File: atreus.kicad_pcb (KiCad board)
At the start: 2 copper layers, 232 x 90 mm, 85 parts

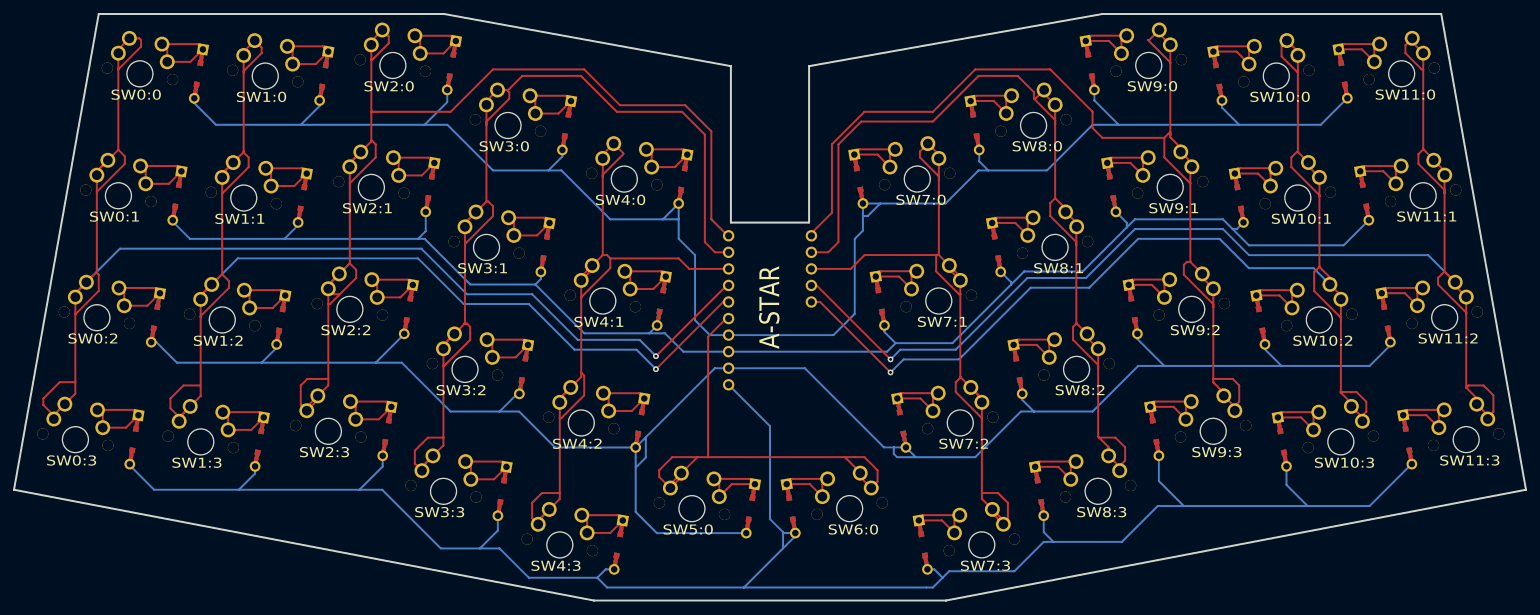
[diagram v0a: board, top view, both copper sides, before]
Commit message: Some Changes:
- Replaced Pololu A-Star with ProMicro.
- Replaced switch footprint with Keebio's switch footprint.
  - Now supports MX, Alps, and Choc.
- Replaced diode footprint with Keebio's switch footprint.
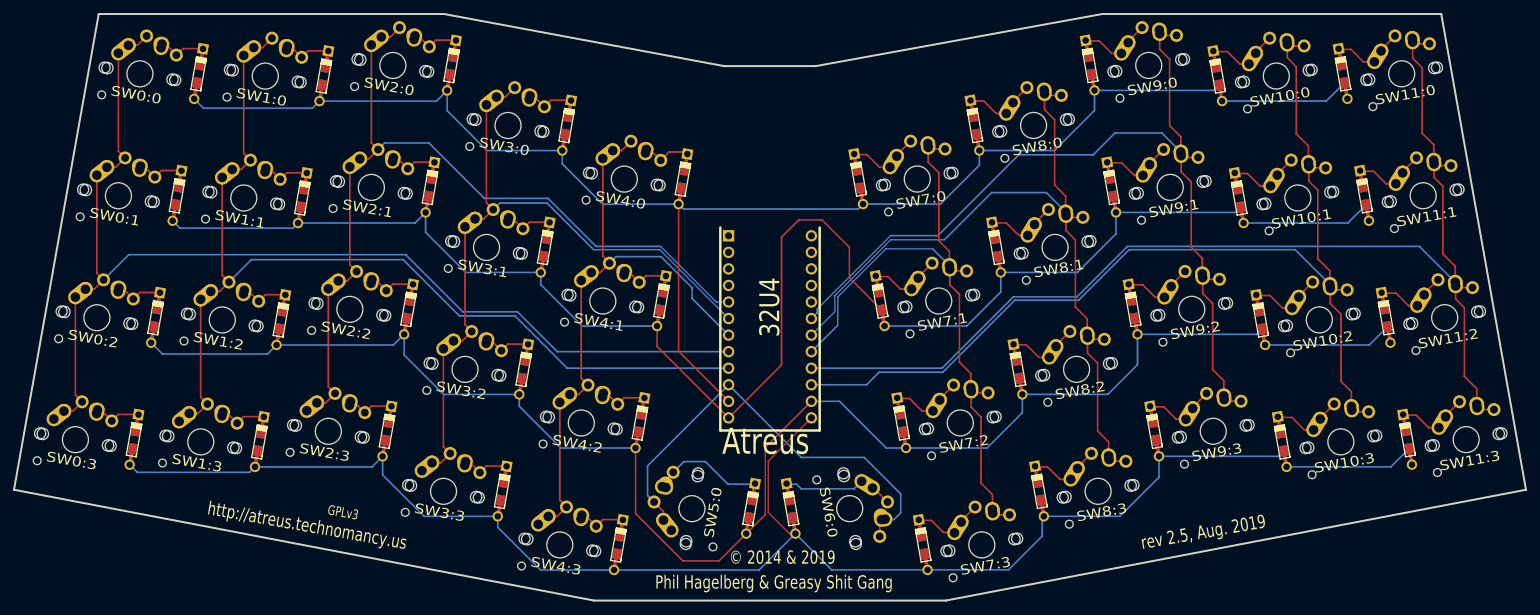
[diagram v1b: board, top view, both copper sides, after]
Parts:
- ?: value A-STAR -> 32U4; footprint A_STAR -> PROMICRO
- SW0:0, SW0:1, SW0:2, SW0:3, SW10:0, SW10:1, SW10:2, SW10:3, SW11:0, SW11:1, SW11:2, SW11:3, SW1:0, SW1:1, SW1:2, SW1:3, SW2:0, SW2:1, SW2:2, SW2:3, SW3:0, SW3:1, SW3:2, SW3:3, SW4:0, SW4:1, SW4:2, SW4:3, SW5:0, SW6:0, SW7:0, SW7:1, SW7:2, SW7:3, SW8:0, SW8:1, SW8:2, SW8:3, SW9:0, SW9:1, SW9:2, SW9:3: footprint MX_FLIP -> Keebio-Parts:MX-Alps-Choc-1U-NoLED
- turned SW5:0 to 80 degrees
- turned SW6:0 to 280 degrees
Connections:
- ? pad B4: N-col-3 -> N-row-0
- ? pad B5: N-col-2 -> N-row-1
- ? pad B6: N-col-6 -> N-row-3
- ? pad C6: N-col-1 -> N-col-0
- ? pad D0: N-row-0 -> N-col-3
- ? pad D1: N-row-1 -> N-col-2
- ? pad D4: N-col-5 -> N-col-4
- ? pad D7: N-col-0 -> N-col-1
- ? pad E6: N-col-4 -> N-col-5
- ? pad F7: N-col-8 -> N-col-6
- D2:2 pad 1: N-row-0 -> N-diode-0
- D2:2 pad 2: N-diode-0 -> N-row-0
- D2:2 pad 1: N-row-1 -> N-diode-9
- D2:2 pad 2: N-diode-9 -> N-row-1
- D2:2 pad 1: N-row-2 -> N-diode-10
- D2:2 pad 2: N-diode-10 -> N-row-2
- D2:2 pad 1: N-row-3 -> N-diode-11
- D2:2 pad 2: N-diode-11 -> N-row-3
- D2:2 pad 1: N-row-0 -> N-diode-12
- D2:2 pad 2: N-diode-12 -> N-row-0
- D2:2 pad 1: N-row-1 -> N-diode-13
- D2:2 pad 2: N-diode-13 -> N-row-1
- D2:2 pad 1: N-row-2 -> N-diode-14
- D2:2 pad 2: N-diode-14 -> N-row-2
- D2:2 pad 1: N-row-3 -> N-diode-15
- D2:2 pad 2: N-diode-15 -> N-row-3
- D2:2 pad 1: N-row-0 -> N-diode-16
- D2:2 pad 2: N-diode-16 -> N-row-0
- D2:2 pad 1: N-row-1 -> N-diode-17
- D2:2 pad 2: N-diode-17 -> N-row-1
- D2:2 pad 1: N-row-2 -> N-diode-18
- D2:2 pad 2: N-diode-18 -> N-row-2
- D2:2 pad 1: N-row-1 -> N-diode-1
- D2:2 pad 2: N-diode-1 -> N-row-1
- D2:2 pad 1: N-row-3 -> N-diode-19
- D2:2 pad 2: N-diode-19 -> N-row-3
- D2:2 pad 1: N-row-2 -> N-diode-20
- D2:2 pad 2: N-diode-20 -> N-row-2
- D2:2 pad 1: N-row-3 -> N-diode-24
- D2:2 pad 2: N-diode-24 -> N-row-3
- D2:2 pad 1: N-row-0 -> N-diode-28
- D2:2 pad 2: N-diode-28 -> N-row-0
- D2:2 pad 1: N-row-1 -> N-diode-29
- D2:2 pad 2: N-diode-29 -> N-row-1
- D2:2 pad 1: N-row-2 -> N-diode-30
- D2:2 pad 2: N-diode-30 -> N-row-2
- D2:2 pad 1: N-row-3 -> N-diode-31
- D2:2 pad 2: N-diode-31 -> N-row-3
- D2:2 pad 1: N-row-0 -> N-diode-32
- D2:2 pad 2: N-diode-32 -> N-row-0
- D2:2 pad 1: N-row-1 -> N-diode-33
- D2:2 pad 2: N-diode-33 -> N-row-1
- D2:2 pad 1: N-row-2 -> N-diode-34
- D2:2 pad 2: N-diode-34 -> N-row-2
- D2:2 pad 1: N-row-2 -> N-diode-2
- D2:2 pad 2: N-diode-2 -> N-row-2
- D2:2 pad 1: N-row-3 -> N-diode-35
- D2:2 pad 2: N-diode-35 -> N-row-3
- D2:2 pad 1: N-row-0 -> N-diode-36
- D2:2 pad 2: N-diode-36 -> N-row-0
- D2:2 pad 1: N-row-1 -> N-diode-37
- D2:2 pad 2: N-diode-37 -> N-row-1
- D2:2 pad 1: N-row-2 -> N-diode-38
- D2:2 pad 2: N-diode-38 -> N-row-2
- D2:2 pad 1: N-row-3 -> N-diode-39
- D2:2 pad 2: N-diode-39 -> N-row-3
- D2:2 pad 1: N-row-0 -> N-diode-40
- D2:2 pad 2: N-diode-40 -> N-row-0
- D2:2 pad 1: N-row-1 -> N-diode-41
- D2:2 pad 2: N-diode-41 -> N-row-1
- D2:2 pad 1: N-row-2 -> N-diode-21
- D2:2 pad 2: N-diode-21 -> N-row-2
- D2:2 pad 1: N-row-3 -> N-diode-22
- D2:2 pad 2: N-diode-22 -> N-row-3
- D2:2 pad 1: N-row-0 -> N-diode-23
- D2:2 pad 2: N-diode-23 -> N-row-0
- D2:2 pad 1: N-row-3 -> N-diode-3
- D2:2 pad 2: N-diode-3 -> N-row-3
- D2:2 pad 1: N-row-1 -> N-diode-25
- D2:2 pad 2: N-diode-25 -> N-row-1
- D2:2 pad 1: N-row-2 -> N-diode-26
- D2:2 pad 2: N-diode-26 -> N-row-2
- D2:2 pad 1: N-row-3 -> N-diode-27
- D2:2 pad 2: N-diode-27 -> N-row-3
- D2:2 pad 1: N-row-0 -> N-diode-4
- D2:2 pad 2: N-diode-4 -> N-row-0
- D2:2 pad 1: N-row-1 -> N-diode-5
- D2:2 pad 2: N-diode-5 -> N-row-1
- D2:2 pad 1: N-row-2 -> N-diode-6
- D2:2 pad 2: N-diode-6 -> N-row-2
- D2:2 pad 1: N-row-3 -> N-diode-7
- D2:2 pad 2: N-diode-7 -> N-row-3
- D2:2 pad 1: N-row-0 -> N-diode-8
- D2:2 pad 2: N-diode-8 -> N-row-0
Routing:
- net N-col-2: track 189.2 -> 127.3 mm
- net N-col-3: track 162.6 -> 106.9 mm
- net N-col-0: track 218.7 -> 166.7 mm, vias 1 -> 0
- net N-row-3: track 299.5 -> 248.1 mm
- net N-col-1: track 197.0 -> 148.0 mm, vias 1 -> 0
- net N-col-8: track 176.2 -> 139.8 mm
- net N-col-4: track 124.1 -> 87.7 mm
- net N-row-2: track 281.8 -> 246.7 mm
- net N-col-10: track 211.5 -> 178.6 mm, vias 1 -> 0
- net N-col-9: track 193.0 -> 160.4 mm, vias 1 -> 0
- net N-col-7: track 153.6 -> 122.3 mm
- net N-row-0: track 264.8 -> 234.0 mm
- net N-col-6: track 124.5 -> 101.4 mm
- net N-row-1: track 226.9 -> 246.4 mm
- net N-col-5: track 80.4 -> 69.3 mm
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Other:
- outline, holes or cut-outs redrawn
- board text added: "Atreus"
- board text added: "GPLv3"
- board text added: "Phil Hagelberg & Greasy Shit Gang"
- board text added: "http://atreus.technomancy.us"
- board text added: "rev 2.5, Aug. 2019"
- board text added: "© 2014 & 2019"

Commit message: brought that space back.
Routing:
- net N-row-0: track 234.0 -> 235.1 mm
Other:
- outline, holes or cut-outs redrawn
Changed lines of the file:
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@@
 (gr_line (start 84 22) (end 127 30) (angle 90) (layer Edge.Cuts) (width 0.3))
 (gr_line (start 141 30) (end 185 22) (angle 90) (layer Edge.Cuts) (width 0.3))
-(gr_line (start 127 30) (end 141 30) (angle 90) (layer Edge.Cuts) (width 0.3))
+(gr_line (start 127 30) (end 127 52) (angle 90) (layer Edge.Cuts) (width 0.3))
+(gr_line (start 127 52) (end 141 52) (angle 90) (layer Edge.Cuts) (width 0.3))
+(gr_line (start 141 30) (end 141 52) (angle 90) (layer Edge.Cuts) (width 0.3))
 (gr_line (start 185 22) (end 237 22) (angle 90) (layer Edge.Cuts) (width 0.3))
 (gr_line (start 237 22) (end 250 95) (angle 90) (layer Edge.Cuts) (width 0.3))
@@
   (segment (start 219.361549 35.35732) (end 222.16846 32.550409) (width 0.254) (layer Back) (net 1) (status 20))
   (segment (start 203.370289 35.35732) (end 219.361549 35.35732) (width 0.254) (layer Back) (net 1) (status 10))
-  (segment (start 147.510752 51.931496) (end 148.278136 51.164112) (width 0.254) (layer Back) (net 1) (status 20))
-  (segment (start 120.730663 51.931496) (end 147.510752 51.931496) (width 0.254) (layer Back) (net 1))
-  (segment (start 119.969379 51.170212) (end 120.730663 51.931496) (width 0.254) (layer Back) (net 1) (status 10))
   (segment (start 119.969379 73.749379) (end 127.65 81.43) (width 0.254) (layer Front) (net 1) (status 20))
   (segment (start 119.969379 51.170212) (end 119.969379 73.749379) (width 0.254) (layer Front) (net 1) (status 10))
+  (segment (start 146.102248 53.34) (end 148.278136 51.164112) (width 0.254) (layer Back) (net 1))
+  (segment (start 119.969379 51.170212) (end 122.139167 53.34) (width 0.254) (layer Back) (net 1))
+  (segment (start 122.139167 53.34) (end 146.102248 53.34) (width 0.254) (layer Back) (net 1))
   (segment (start 42.345619 53.729875) (end 43.479744 54.864) (width 0.254) (layer Back) (net 2) (status 10))
   (segment (start 60.788677 54.864) (end 61.57791 54.074767) (width 0.254) (layer Back) (net 2) (status 20))

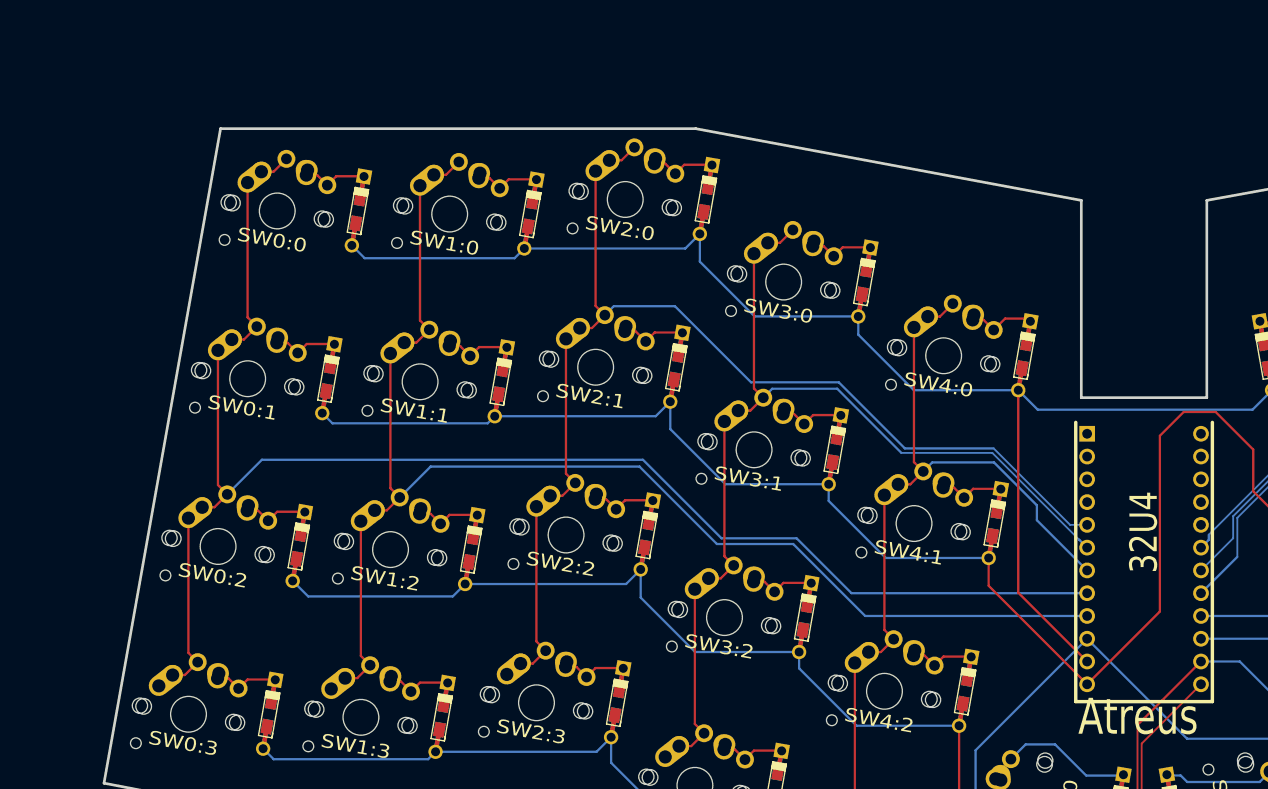
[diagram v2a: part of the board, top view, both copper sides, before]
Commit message: starting to add some smd modules.
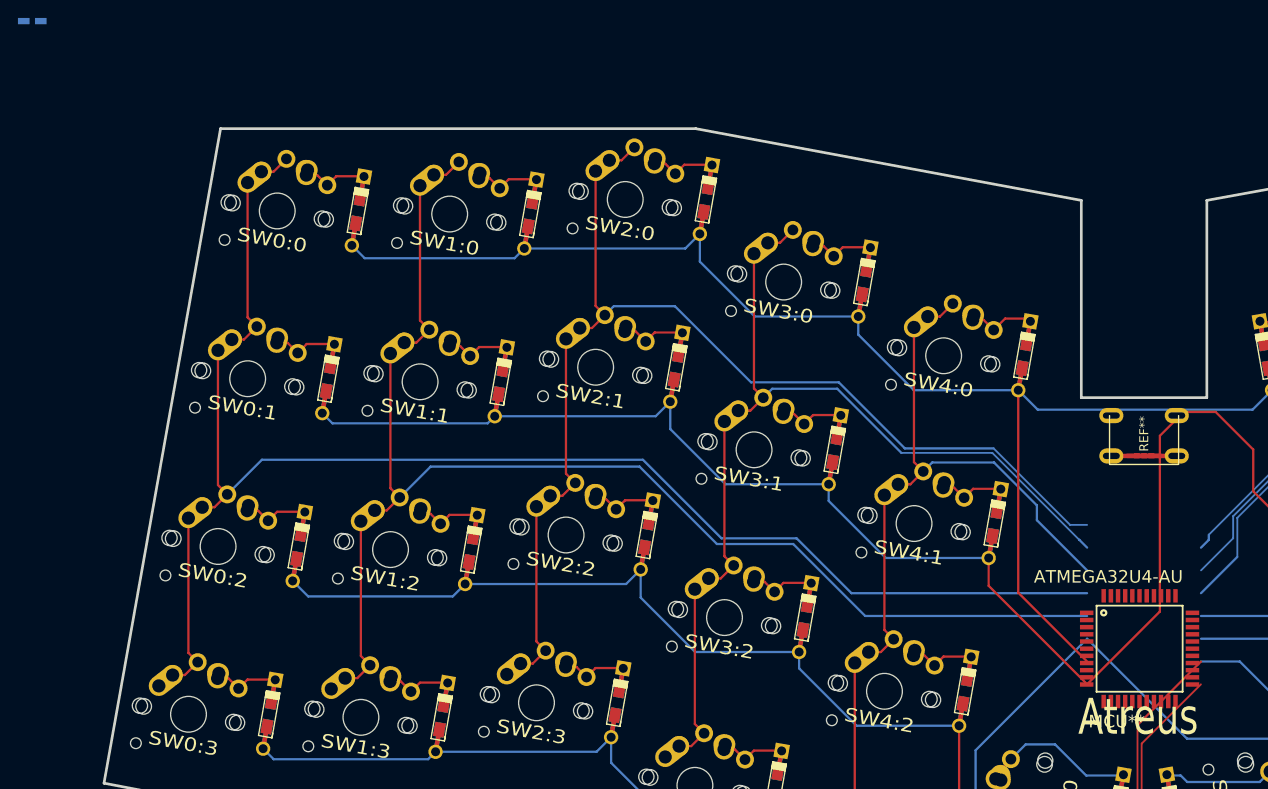
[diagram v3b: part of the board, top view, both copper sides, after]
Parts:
- removed ?: 32U4, PROMICRO
- added ATMEGA32U4-AU: MCU**, ATMEGA32U4-AU, F.Cu at (133.5, 80.0)
- added R22: 22, Resistors_SMD:R_0805, B.Cu at (10.0, 10.0)
- added REF**: Molex-0548190589, Molex-0548190589, F.Cu at (134.0, 54.0)

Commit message: something else.
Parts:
- removed ATMEGA32U4-AU: MCU**, ATMEGA32U4-AU
- added U1: ATmega32U4-AU, ATMEGA32U4-AU, F.Cu at (133.5, 80.0)
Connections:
- R22 pad 1: N-GND -> GND
- R22 pad 2: N-C1-P1 -> Net-C1-Pad1
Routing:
- net N-row-3: track 248.1 -> 0.00 mm
- net N-row-2: track 246.7 -> 0.00 mm
- net N-row-1: track 246.4 -> 0.00 mm
- net N-row-0: track 235.1 -> 0.00 mm
- net N-col-10: track 178.6 -> 0.00 mm
- net N-col-0: track 166.7 -> 0.00 mm
- net N-col-9: track 160.4 -> 0.00 mm
- net N-col-1: track 148.0 -> 0.00 mm
- net N-col-8: track 139.8 -> 0.00 mm
- net N-col-2: track 127.3 -> 0.00 mm
- net N-col-7: track 122.3 -> 0.00 mm
- net N-col-3: track 106.9 -> 0.00 mm
- net N-col-6: track 101.4 -> 0.00 mm
- net N-col-4: track 87.7 -> 0.00 mm
- net N-col-5: track 69.3 -> 0.00 mm
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
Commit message: added usb mini and crystal.
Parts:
- removed R22: 22, Resistors_SMD:R_0805
- added C1: 22pf, Capacitors_SMD:C_0805, B.Cu at (0.00, 0.00)
- added C2: 22pf, Capacitors_SMD:C_0805, B.Cu at (10.0, 0.00)
- added Y1: Crystal_GND24_Small, Crystals:Crystal_SMD_3225-4pin_3.2x2.5mm, B.Cu at (5.00, 0.00)
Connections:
- REF** pad 1: (no net) -> GND
- REF** pad 2: (no net) -> Net-USB1-Pad2
- REF** pad 3: (no net) -> D+
- REF** pad 4: (no net) -> D-
- REF** pad 5: (no net) -> VCC
- U1 pad 1: Net-U1-Pad1 -> N-col-5
- U1 pad 10: Net-U1-Pad10 -> N-row-2
- U1 pad 11: Net-U1-Pad11 -> N-col-9
- U1 pad 18: Net-U1-Pad18 -> N-col-3
- U1 pad 19: Net-U1-Pad19 -> N-col-2
- U1 pad 25: Net-U1-Pad25 -> N-col-4
- U1 pad 27: (no net) -> N-col-1
- U1 pad 28: (no net) -> N-row-0
- U1 pad 29: (no net) -> N-row-1
- U1 pad 30: (no net) -> N-row-3
- U1 pad 31: Net-U1-Pad31 -> N-col-0
- U1 pad 36: Net-U1-Pad36 -> N-col-6
- U1 pad 37: Net-U1-Pad37 -> N-col-7
- U1 pad 38: Net-U1-Pad38 -> N-col-8
- U1 pad 9: Net-U1-Pad9 -> N-col-10
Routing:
- net N-row-3: track 0.00 -> 248.1 mm
- net N-row-2: track 0.00 -> 246.7 mm
- net N-row-1: track 0.00 -> 246.4 mm
- net N-row-0: track 0.00 -> 235.1 mm
- net N-col-10: track 0.00 -> 178.6 mm
- net N-col-0: track 0.00 -> 166.7 mm
- net N-col-9: track 0.00 -> 160.4 mm
- net N-col-1: track 0.00 -> 148.0 mm
- net N-col-8: track 0.00 -> 139.8 mm
- net N-col-2: track 0.00 -> 127.3 mm
- net N-col-7: track 0.00 -> 122.3 mm
- net N-col-3: track 0.00 -> 106.9 mm
- net N-col-6: track 0.00 -> 101.4 mm
- net N-col-4: track 0.00 -> 87.7 mm
- net N-col-5: track 0.00 -> 69.3 mm
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
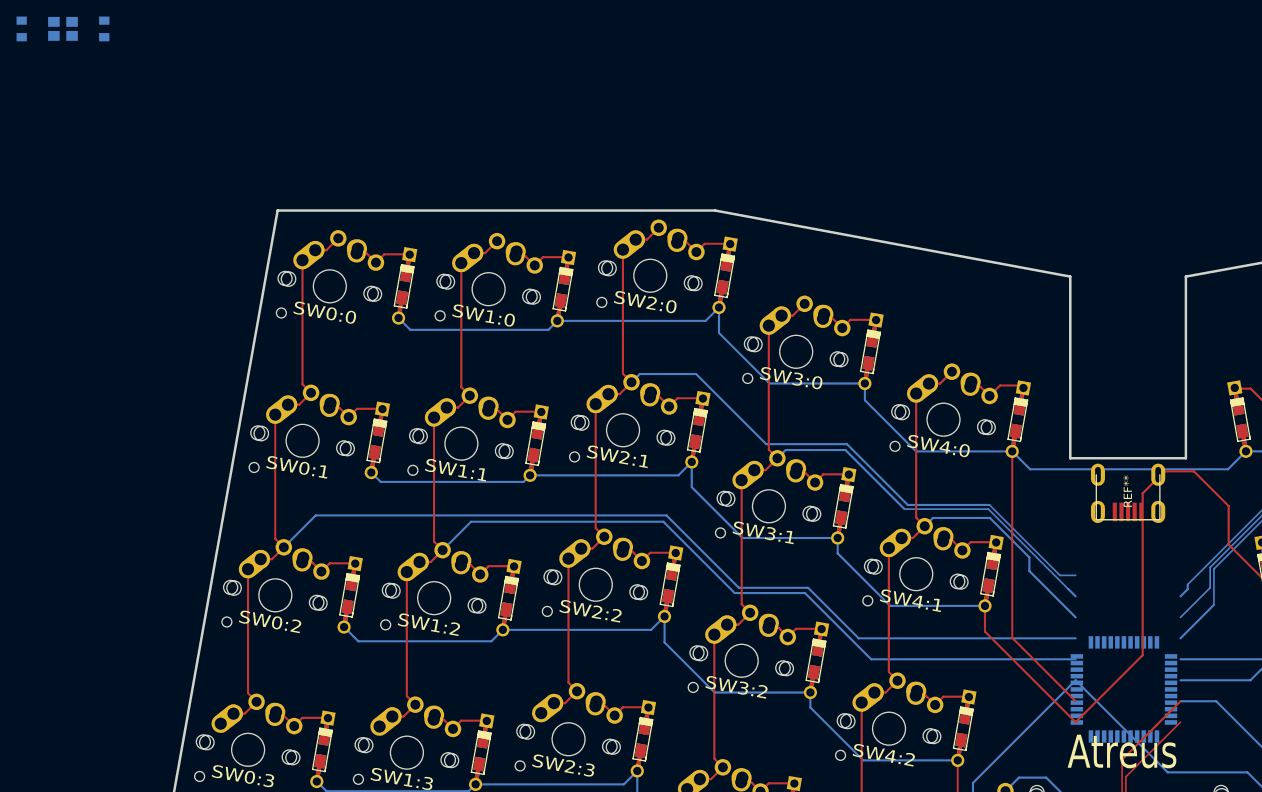
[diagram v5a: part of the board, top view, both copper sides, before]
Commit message: miniusb, atmega, and crystal placements.
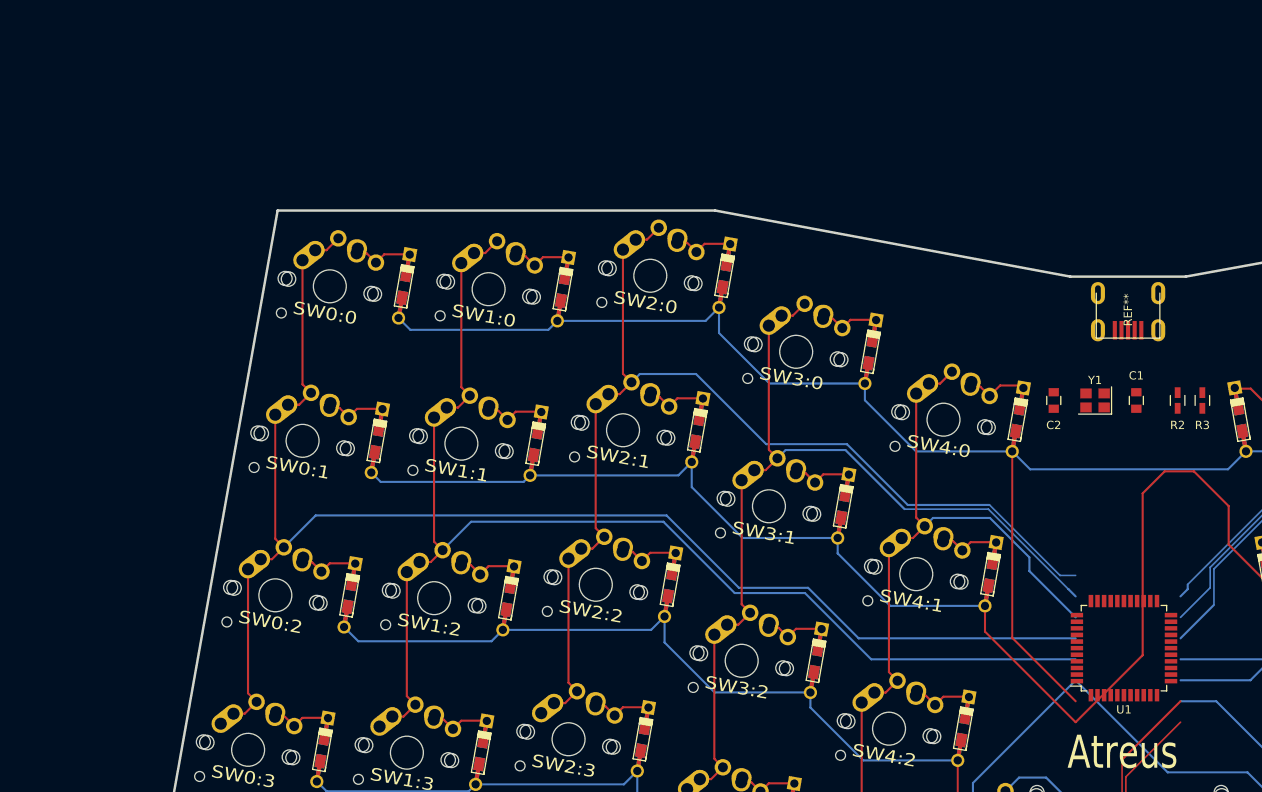
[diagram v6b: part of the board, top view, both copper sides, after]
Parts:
- added R2: 22, Resistors_SMD:R_0805, F.Cu at (140.0, 45.0)
- added R3: 22, Resistors_SMD:R_0805, F.Cu at (143.0, 45.0)
- C1, C2, Y1: moved to F.Cu
- moved C1 142.3 mm to (135.0, 45.0), turned to 270 degrees
- moved Y1 132.9 mm to (130.0, 45.0), turned to 180 degrees
- moved C2 123.5 mm to (125.0, 45.0), turned to 90 degrees
- moved REF** 22.0 mm to (134.0, 32.0)
- moved U1 5.00 mm to (133.5, 75.0)
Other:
- outline, holes or cut-outs redrawn
